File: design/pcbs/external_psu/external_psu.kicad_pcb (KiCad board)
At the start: 2 copper layers, 135 x 110 mm, 40 parts

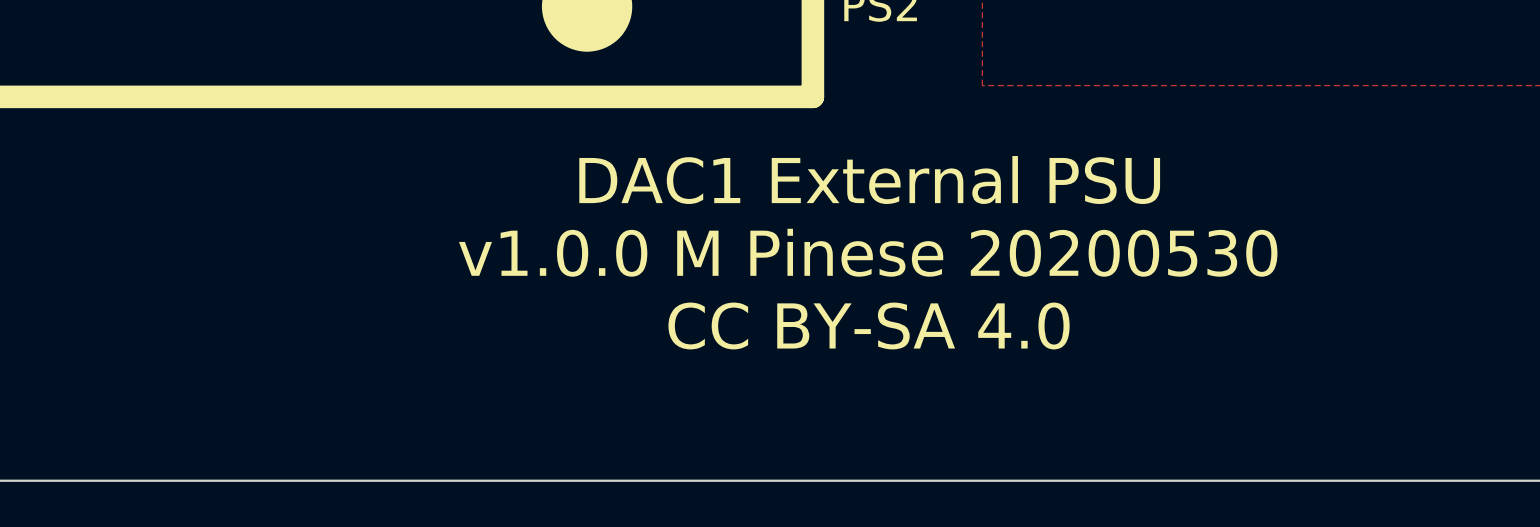
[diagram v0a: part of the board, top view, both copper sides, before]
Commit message: Updated PCB sheet info. Clarified licence in readme.
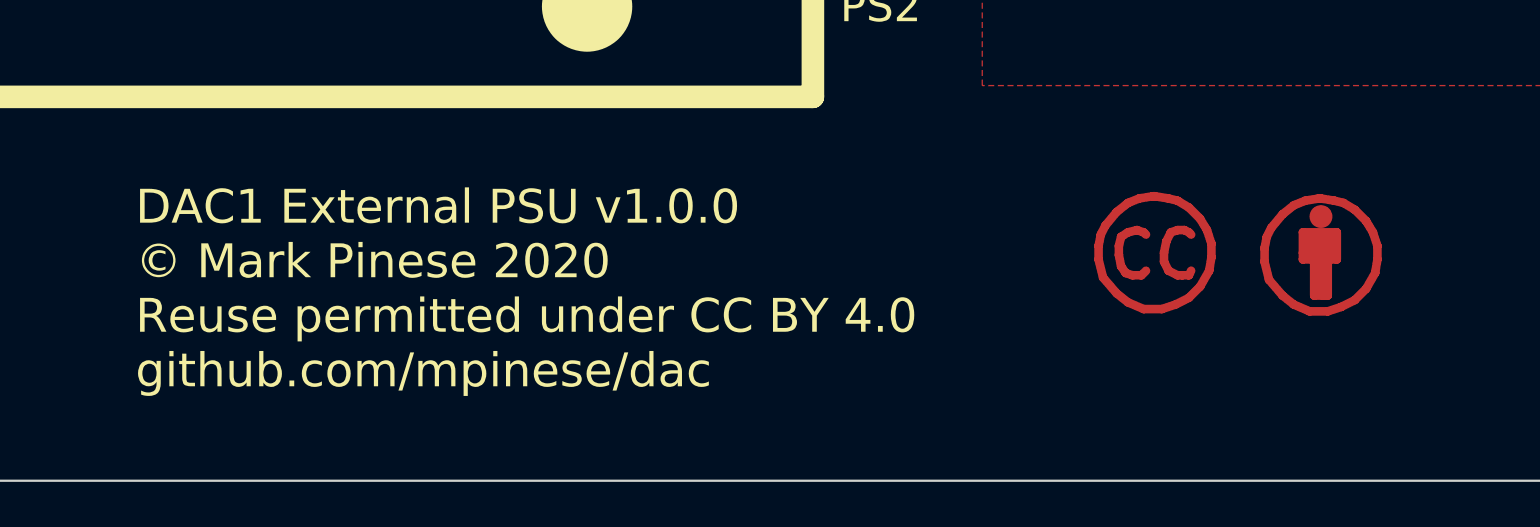
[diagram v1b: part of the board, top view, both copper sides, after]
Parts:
- added REF**: Symbol_CC-Attribution_CopperTop_Small, Symbol:Symbol_CC-Attribution_CopperTop_Small, F.Cu at (162.5, 140.0)
- added REF**: Symbol_CreativeCommons_CopperTop_Type2_Small, Symbol:Symbol_CreativeCommons_CopperTop_Type2_Small, F.Cu at (155.0, 140.0)
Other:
- board text added: "DAC1 External PSU v1.0.0 © Mark Pinese 2020 Reuse permitted under CC BY 4.0 github.com/mpinese/dac"
- board text removed: "1.0.0"
- board text removed: "1/1"
- board text removed: "20200530"
- board text removed: "Author: Mark Pinese"
- board text removed: "DAC1 External PSU"
- board text removed: "DAC1 External PSU v1.0.0 M Pinese 20200530 CC BY-SA 4.0"
- board text removed: "This work is licensed under CC BY-SA 4.0. To view a copy of this license, visit https://creativecommons.org/licenses/by-sa/4.0"

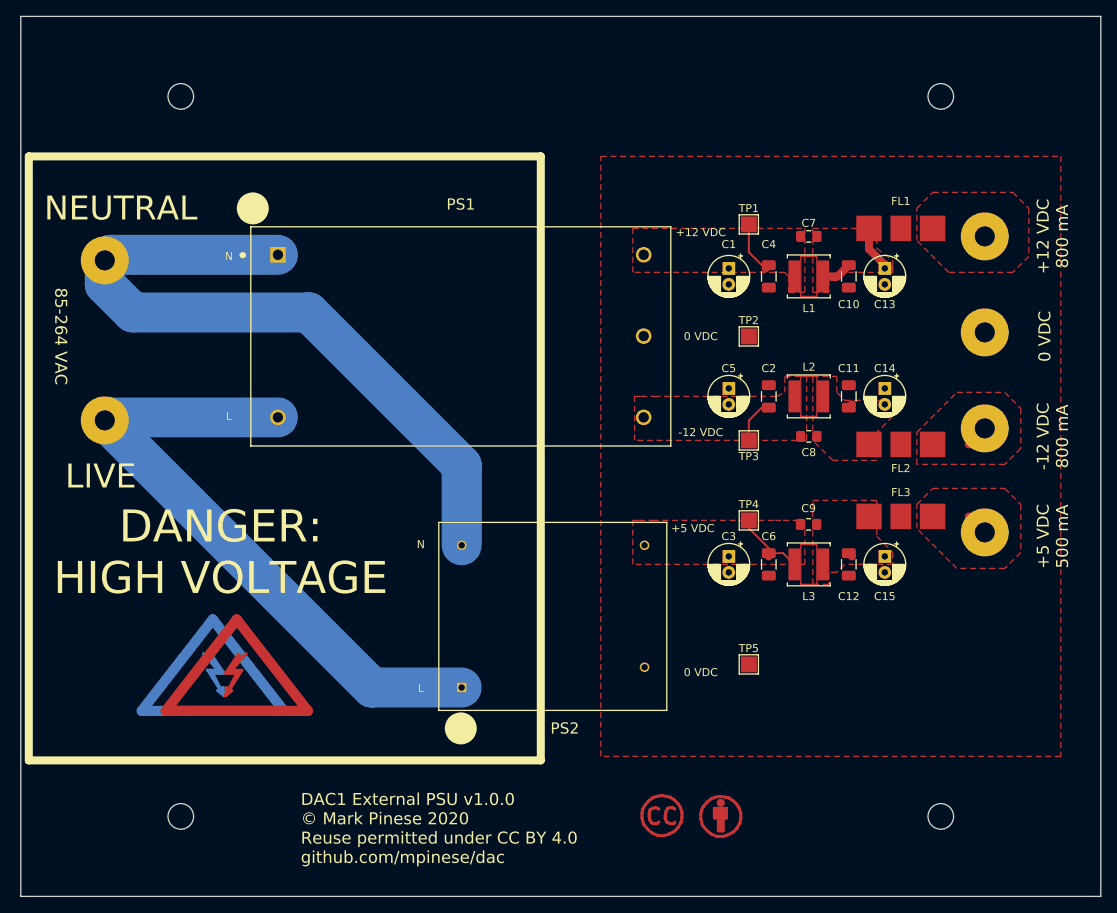
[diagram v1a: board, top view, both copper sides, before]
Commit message: Fixed title blocks. Added fab outputs.
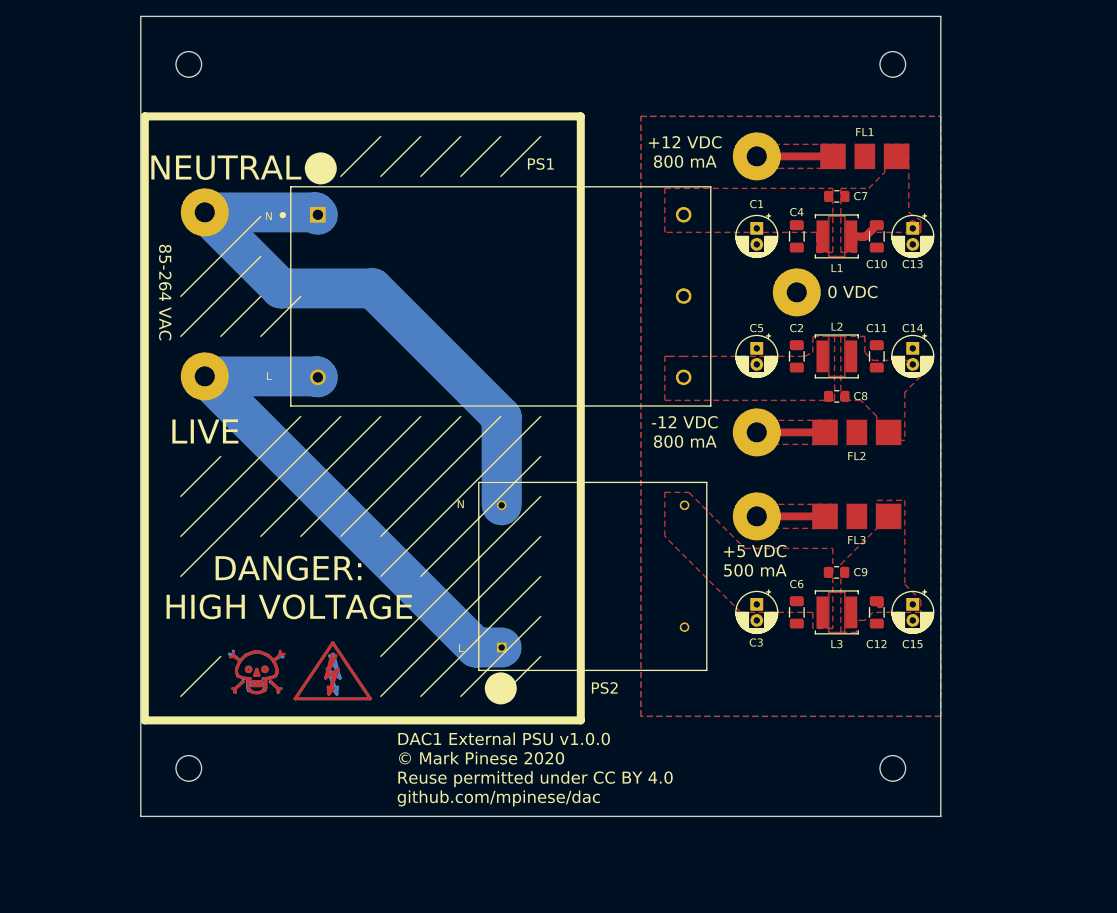
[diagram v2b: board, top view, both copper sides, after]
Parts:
- removed the REF** at (162.5, 140.0)
- removed the REF** at (155.0, 140.0)
- removed the REF** at (99.0, 123.0)
- removed the REF** at (102.0, 123.0)
- removed TP1, TP2, TP3, TP4, TP5: TestPoint, TestPoint:TestPoint_Pad_2.0x2.0mm
- added REF**: Symbol_HighVoltage_Type2_CopperTop_VerySmall, Symbol:Symbol_HighVoltage_Type2_CopperTop_VerySmall, F.Cu at (114.0, 122.5)
- added REF**: Symbol_Danger_CopperTop_Small, Symbol:Symbol_Danger_CopperTop_Small, F.Cu at (104.5, 122.0)
- added REF**: Symbol_HighVoltage_Type2_CopperTop_VerySmall, Symbol:Symbol_HighVoltage_Type2_CopperTop_VerySmall, B.Cu at (114.0, 122.5)
- added REF**: Symbol_Danger_CopperTop_Small, Symbol:Symbol_Danger_CopperTop_Small, B.Cu at (104.5, 122.0)
- moved CONN3 30.2 mm to (167.0, 57.5)
- moved CONN6 28.6 mm to (167.0, 102.5)
- moved CONN5 28.5 mm to (167.0, 92.0)
- moved CONN4 24.0 mm to (172.0, 74.5)
- moved CONN2 13.9 mm to (98.0, 64.5)
- moved CONN1 13.7 mm to (98.0, 85.0)
- moved FL1 10.1 mm to (180.5, 57.5), turned to 180 degrees
- moved H4 8.49 mm to (184.0, 134.0)
- moved H3 7.21 mm to (184.0, 46.0)
- moved PS1 7.07 mm to (135.0, 75.0)
- moved PS2 7.07 mm to (146.5, 110.0)
- moved C12 6.95 mm to (182.0, 114.5)
- moved C15 6.95 mm to (186.5, 113.5)
- moved C3 6.95 mm to (167.0, 113.5)
- moved C6 6.95 mm to (172.0, 114.5)
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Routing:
- net /NEUTRAL: track 88.9 -> 73.0 mm
- net /LIVE: track 80.2 -> 65.3 mm
- net Net-(C3-Pad1): track 9.31 -> 0.00 mm
- net Net-(CONN3-Pad1): track 1.41 -> 9.53 mm
- net Net-(C1-Pad1): track 7.21 -> 0.00 mm
- net Net-(CONN6-Pad1): track 2.83 -> 8.53 mm
- net Net-(CONN5-Pad1): track 2.83 -> 8.53 mm
- net Net-(C2-Pad2): track 5.65 -> 0.00 mm
- net Net-(C10-Pad1): track 10.2 -> 4.91 mm
- net Net-(C11-Pad1): track 0.57 -> 0.00 mm
- added copper zone on B.Cu, net GND
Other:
- board size 135 x 110 mm -> 100 x 100 mm
- board text removed: "+12 VDC"
- board text removed: "+5 VDC"
- board text removed: "-12 VDC"
